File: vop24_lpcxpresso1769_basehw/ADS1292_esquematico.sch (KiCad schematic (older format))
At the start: 50 parts, among them J401 Conn_01x02, J402 Conn_01x02, J403 Conn_01x02, J404 Conn_01x04, J405 Conn_01x04, J406 Conn_01x04, U401 ADS1292, U402 LM334, U403 LM334, U404 LM334

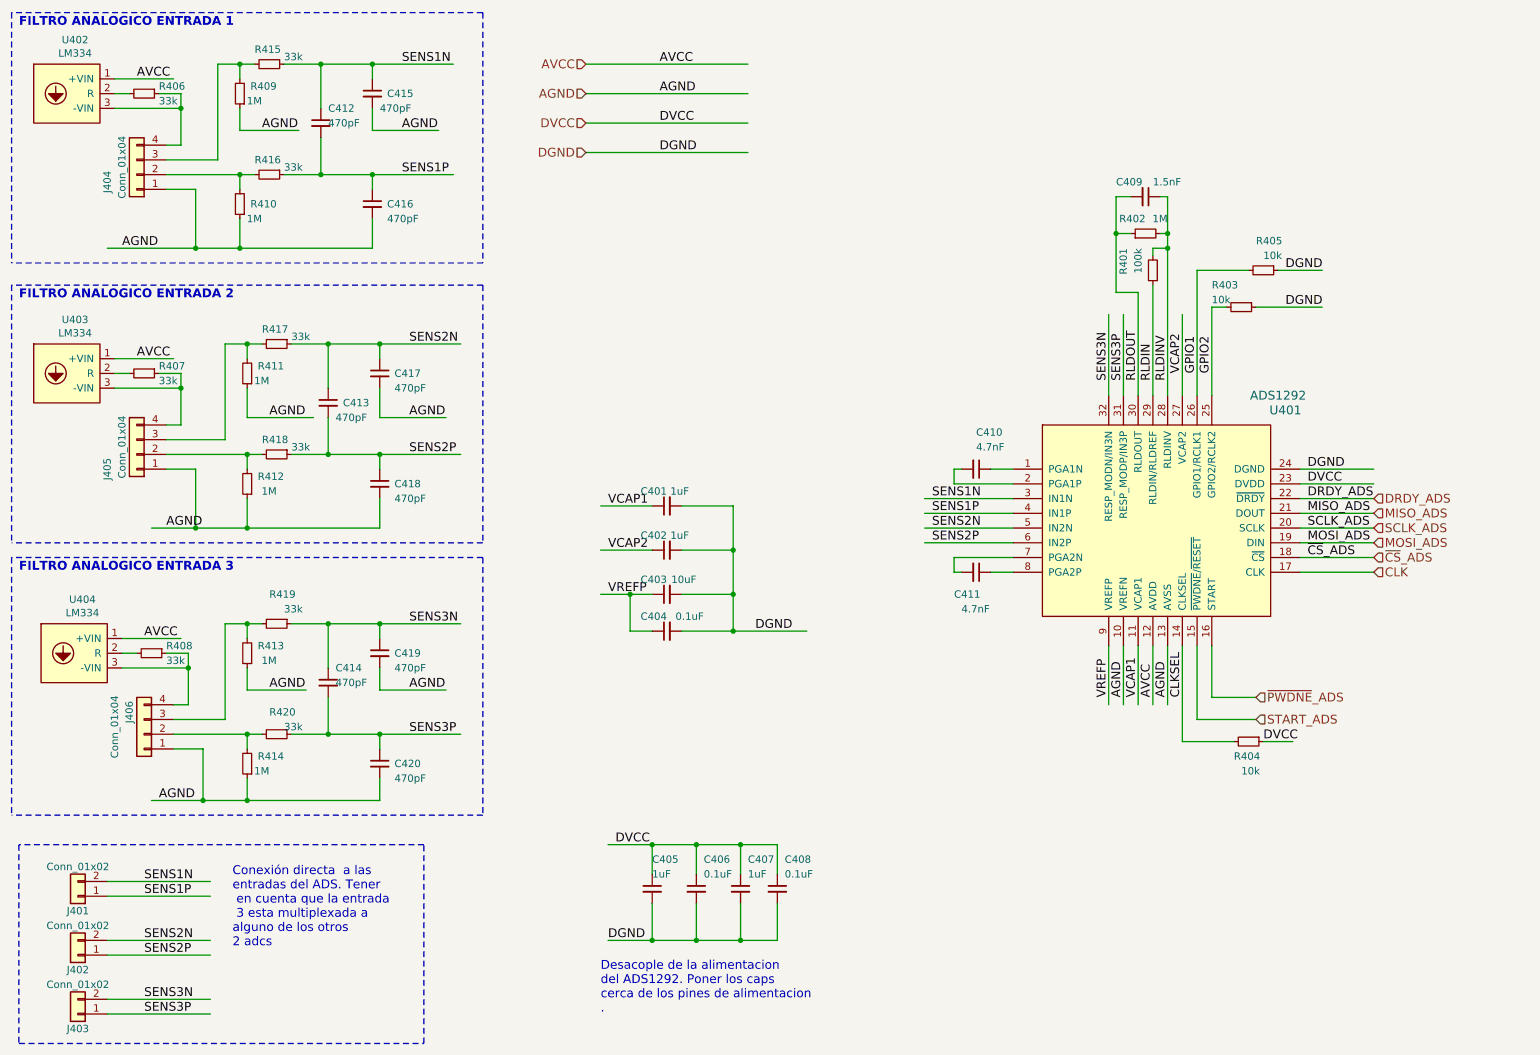
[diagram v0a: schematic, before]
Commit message: ESQ: todas las correcciones atendidas
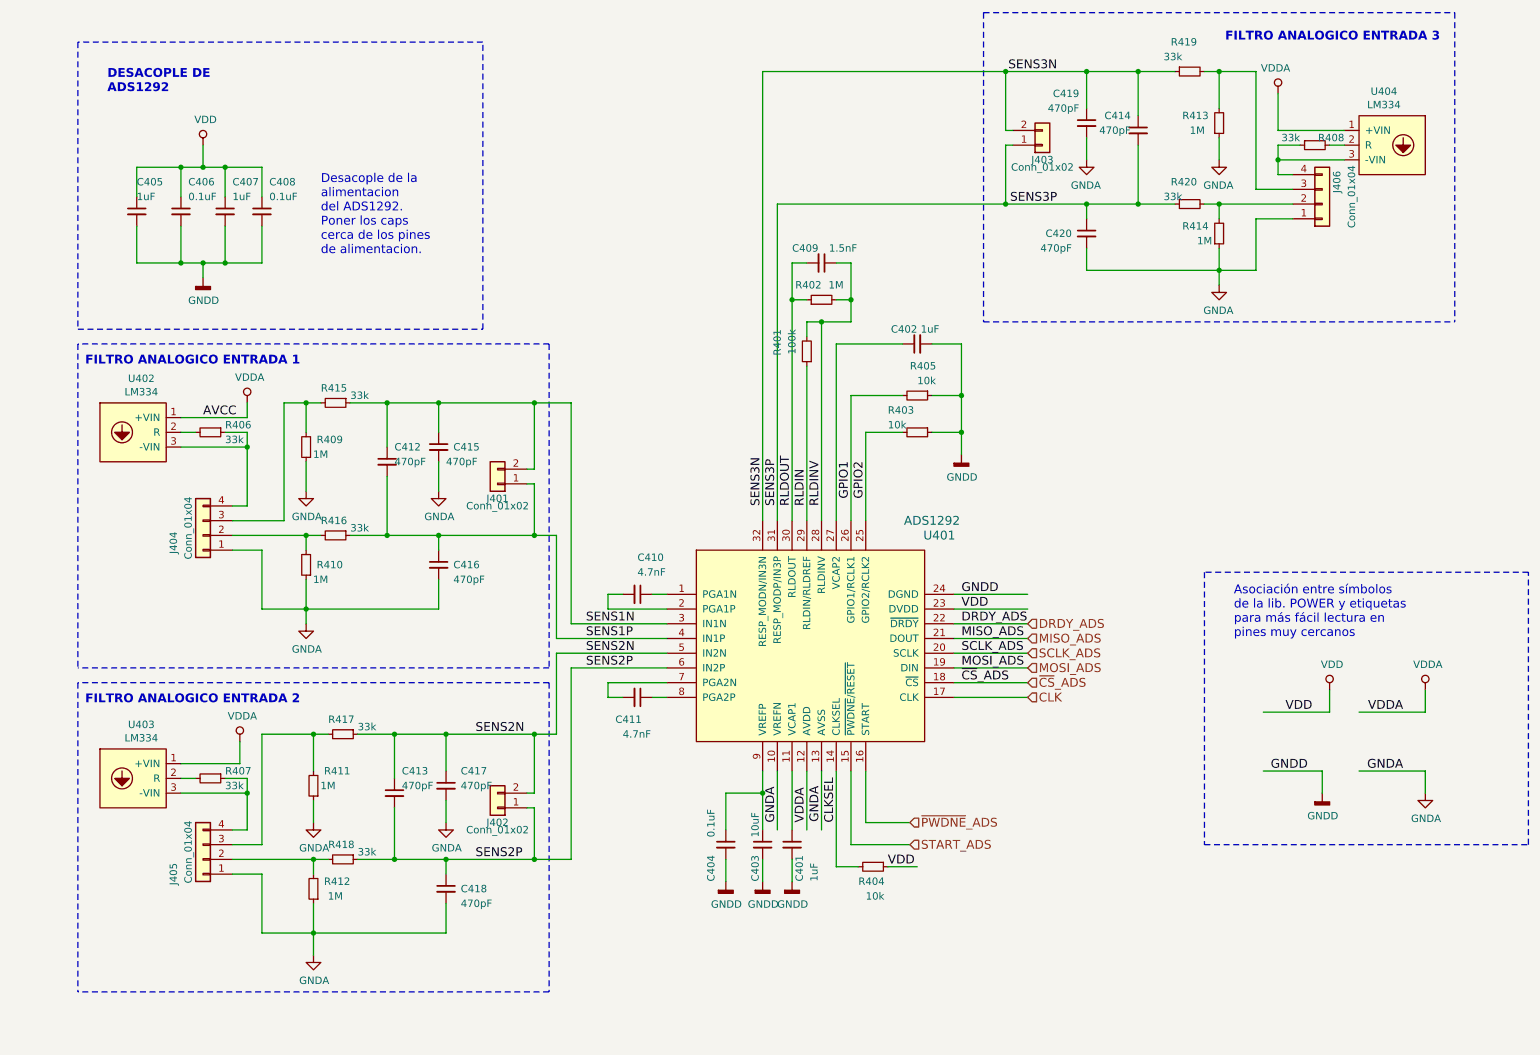
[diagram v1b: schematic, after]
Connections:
- net labels added: GNDA, GNDD, VDD, VDDA
- net labels removed: AGND, DGND, DVCC, VCAP1, VCAP2, VREFP
- wire segments 203 -> 218
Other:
- note added: "Asociación entre símbolos\nde la lib. POWER y etiquetas\npara más fácil lectura en \npines muy cercanos"
- note added: "DESACOPLE DE \nADS1292"
- note added: "Desacople de la \nalimentacion\ndel ADS1292. \nPoner los caps\ncerca de los pines\nde alimentacion."
- note removed: "Conexión directa a las \nentradas del ADS. Tener\n en cuenta que la entrada\n 3 esta multiplexada a \nalguno de los otros \n2 adcs\n"
- note removed: "Desacople de la alimentacion\ndel ADS1292. Poner los caps\ncerca de los pines de alimentacion\n."
- moved on the sheet: C401, C402, C403, C404, C405, C406, C407, C408, C409, C410, C411, C412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
